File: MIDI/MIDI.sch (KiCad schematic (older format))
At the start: 0 parts

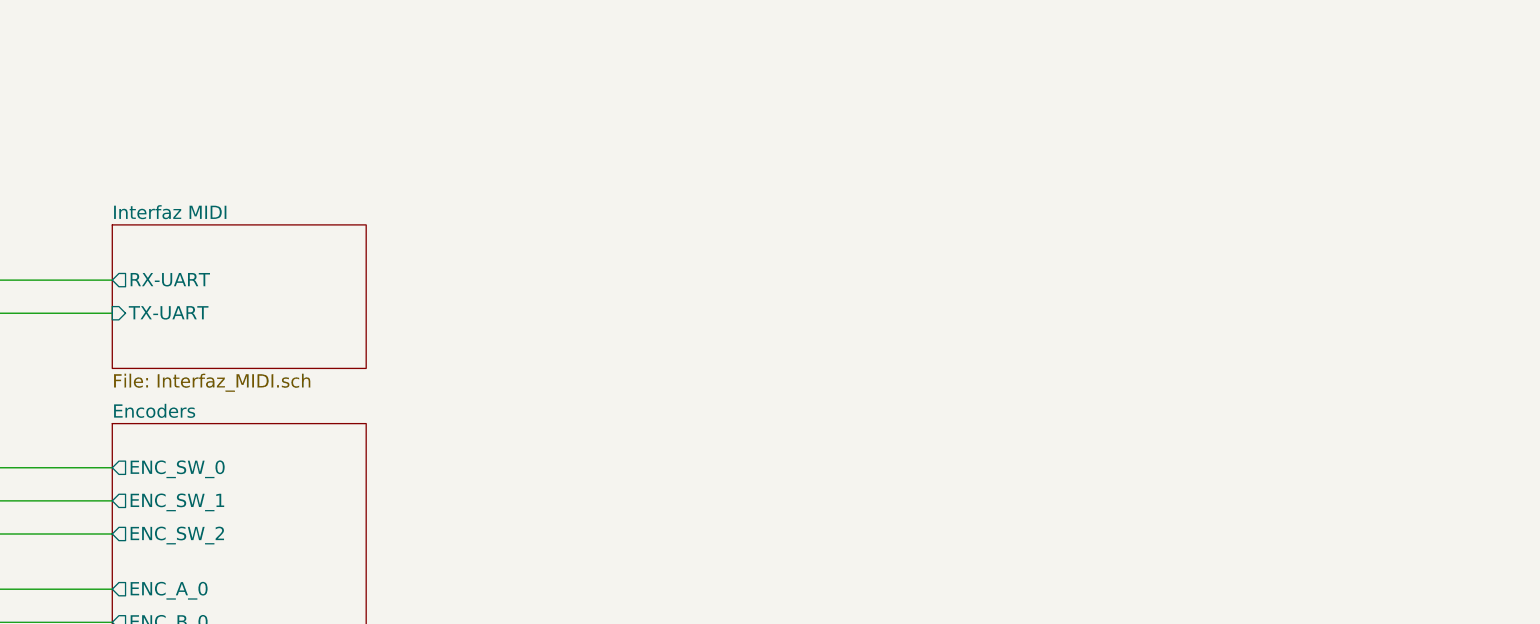
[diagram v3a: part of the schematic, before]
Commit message: Se prosigue el trabajo en el esquemático
> Se incluyen campos utilizados por KiCost en los componentes.
> Se corrigen errores menores.
> Se asignan algunos valores pendientes.
> Se mejoran los rótulos.
> Detalles cosméticos.
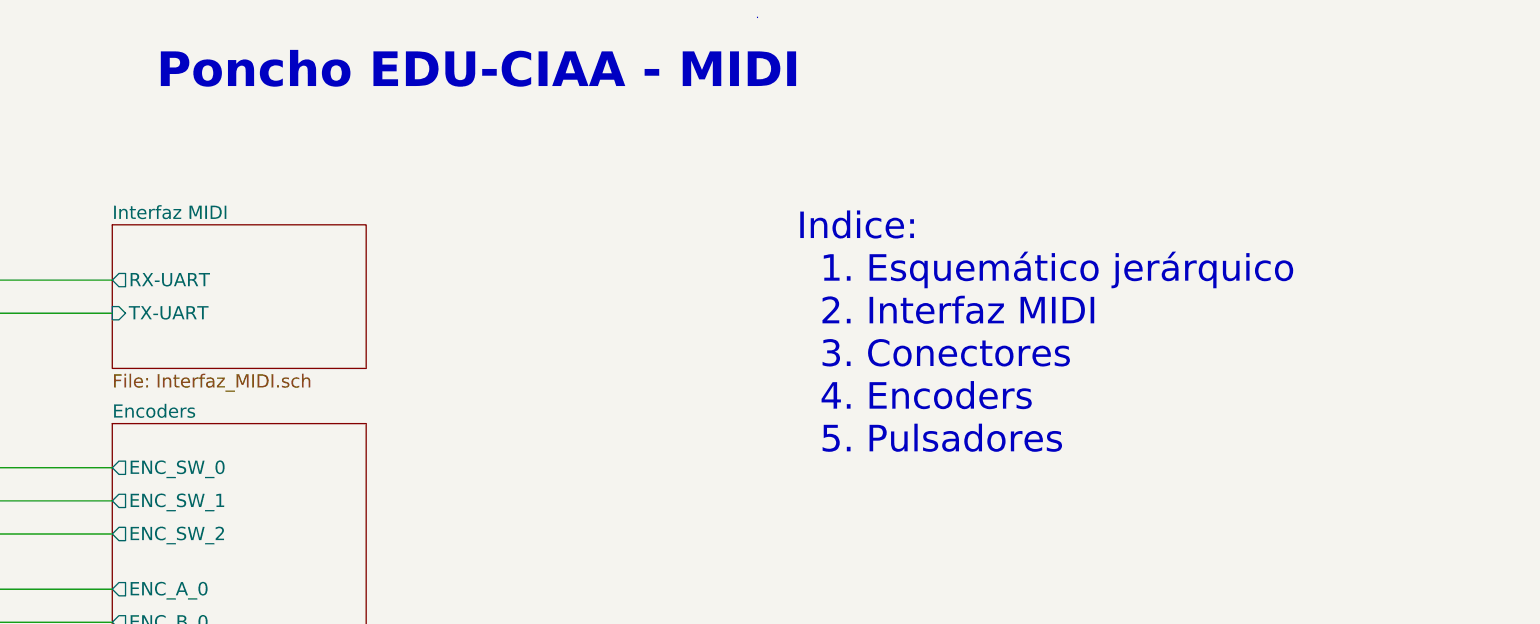
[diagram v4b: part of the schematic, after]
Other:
- note added: "Indice:\n 1. Esquemático jerárquico\n 2. Interfaz MIDI\n 3. Conectores\n 4. Encoders\n 5. Pulsadores"
- note added: "Poncho EDU-CIAA - MIDI"
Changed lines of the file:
@@
 Rev "v0.1"
 Comp "FIUBA - LSE - CESE                                                        Licencia: BSD"
-Comment1 "Autor: Carlos I. Mancón"
-Comment2 ""
+Comment1 "Revisores: Marcelo Moreno  /  Diego Brengi"
+Comment2 "Autor: Carlos I. Mancón"
 Comment3 ""
 Comment4 ""
@@
 Wire Wire Line
 	3250 6550 4050 6550
+Wire Notes Line
+	6970 710  6975 710
+Text Notes 7150 2700 0    120  ~ 0
+Indice:\n  1. Esquemático jerárquico\n  2. Interfaz MIDI\n  3. Conectores\n  4. Encoders\n  5. Pulsadores
+Text Notes 4250 1050 0    157  ~ 31
+Poncho EDU-CIAA - MIDI
 $EndSCHEMATC
